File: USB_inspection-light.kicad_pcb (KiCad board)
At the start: 2 copper layers, 82.8 x 13 mm, 24 parts, among them CON1 USB-MINI-B, IC1 MADW__ATTINY13-MM, Q1 MOSFET_N, SW1 SW_PUSH, SW2 SW_PUSH

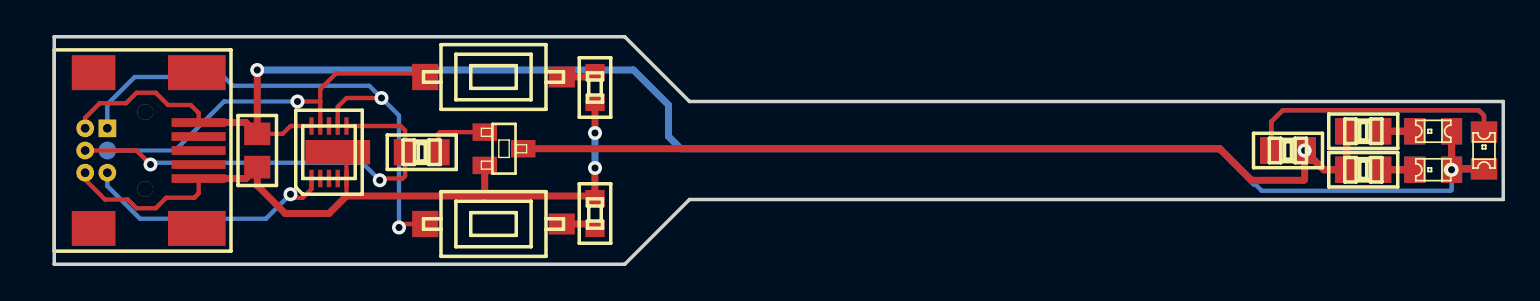
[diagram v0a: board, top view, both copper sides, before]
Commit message: Added a GND plane on F_Cu. Just for fun.
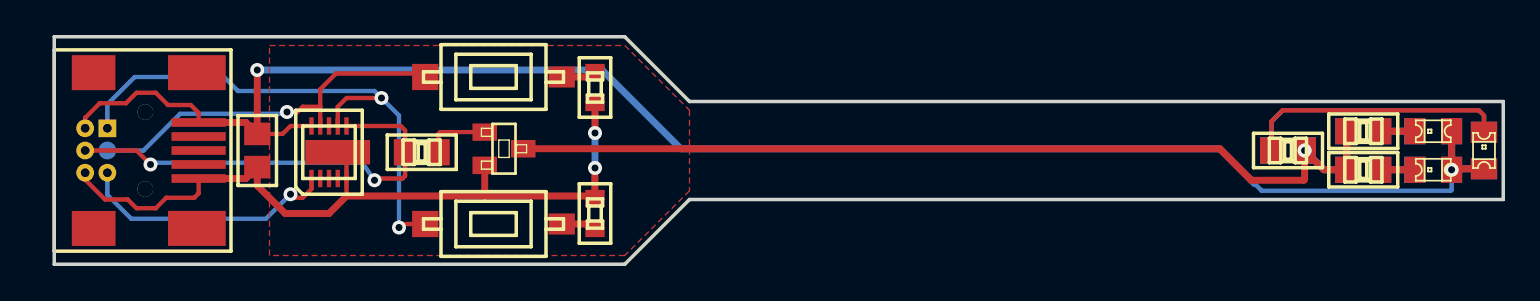
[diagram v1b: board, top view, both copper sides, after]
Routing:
- net +5V: track 101.5 -> 100.5 mm
- added copper zone on F.Cu, net GND
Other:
- board text added: "V0.10.b"
- board text removed: "V0.10.a"

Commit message: GND plane tweaks.
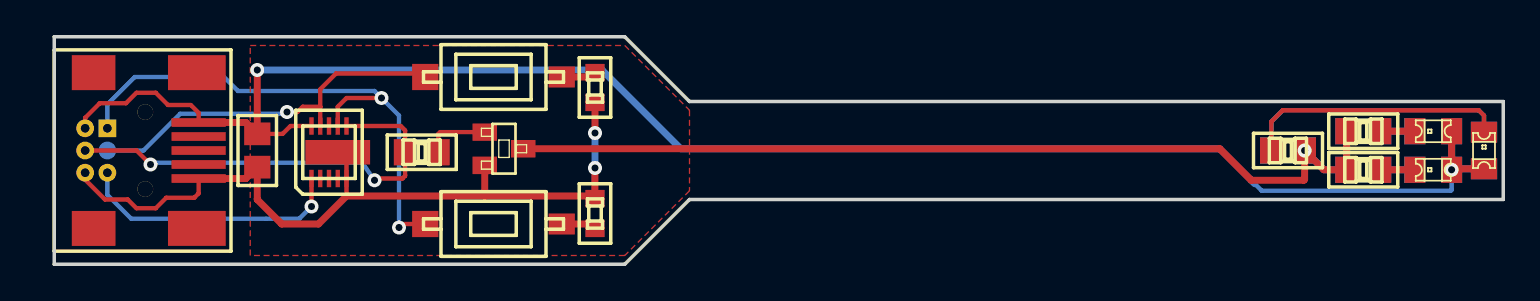
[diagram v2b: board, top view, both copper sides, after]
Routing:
- net GND: track 46.0 -> 46.9 mm
- net /RESET: track 15.0 -> 15.7 mm
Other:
- board text added: "V0.10.c"
- board text removed: "V0.10.b"
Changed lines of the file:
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@@
-(kicad_pcb (version 3) (host pcbnew "(2014-03-01 BZR 4730)-product")
+(kicad_pcb (version 3) (host pcbnew "(2014-02-28 BZR 4729)-product")
   (general
     (links 38)
@@
     (thickness 1.6)
     (drawings 12)
-    (tracks 149)
+    (tracks 148)
     (zones 0)
     (modules 24)
@@
   (title_block
     (title "USB inspection light")
-    (date "02 Mar 2014")
-    (rev 0.10.b)
+    (date "03 Mar 2014")
+    (rev 0.10.c)
     (company "2014 - blog.spitzenpfeil.org")
   )
@@
   )
   (setup
-    (last_trace_width 0.4)
+    (last_trace_width 0.25)
     (user_trace_width 0.25)
     (user_trace_width 0.5)
@@
   (gr_line (start 60.8 102) (end 64.5 105.7) (angle 90) (layer Edge.Cuts) (width 0.2))
   (gr_line (start 111 111.3) (end 111 105.7) (angle 90) (layer Edge.Cuts) (width 0.2))
-  (gr_text V0.10.b (at 78.2 109.9) (layer B.SilkS)
+  (gr_text V0.10.c (at 78.2 109.9) (layer B.SilkS)
     (effects (font (size 1.5 1.5) (thickness 0.3)) (justify mirror))
   )
@@
   (segment (start 48.25004 107.35004) (end 48.25004 108.6) (width 0.25) (layer F.Cu) (net 3) (status 20))
   (segment (start 48 107.1) (end 48.25004 107.35004) (width 0.25) (layer F.Cu) (net 3))
-  (segment (start 31.235 109.77) (end 31.235 111.035) (width 0.25) (layer B.Cu) (net 4) (status 10))
-  (segment (start 42.9 110.7) (end 42.9 110.1) (width 0.25) (layer F.Cu) (net 4) (status 20))
-  (segment (start 42.4 111.2) (end 42.9 110.7) (width 0.25) (layer F.Cu) (net 4))
-  (segment (start 41.9 111.2) (end 42.4 111.2) (width 0.25) (layer F.Cu) (net 4))
-  (segment (start 41.7 111) (end 41.9 111.2) (width 0.25) (layer F.Cu) (net 4))
-  (via (at 41.7 111) (size 0.8) (layers F.Cu B.Cu) (net 4))
-  (segment (start 40.3 112.4) (end 41.7 111) (width 0.25) (layer B.Cu) (net 4))
+  (segment (start 42.9 111.7) (end 42.9 110.1) (width 0.25) (layer F.Cu) (net 4))
+  (segment (start 40.3 112.4) (end 42.2 112.4) (width 0.25) (layer B.Cu) (net 4))
+  (segment (start 31.235 111.035) (end 32.6 112.4) (width 0.25) (layer B.Cu) (net 4))
   (segment (start 32.6 112.4) (end 40.3 112.4) (width 0.25) (layer B.Cu) (net 4))
-  (segment (start 31.235 111.035) (end 32.6 112.4) (width 0.25) (layer B.Cu) (net 4))
+  (via (at 42.9 111.7) (size 0.8) (layers F.Cu B.Cu) (net 4))
+  (segment (start 43.1 111.9) (end 42.9 111.7) (width 0.25) (layer F.Cu) (net 4))
+  (segment (start 31.235 111.035) (end 31.235 109.77) (width 0.25) (layer B.Cu) (net 4) (status 10))
+  (segment (start 42.2 112.4) (end 42.9 111.7) (width 0.25) (layer B.Cu) (net 4))
   (segment (start 31.235 108.5) (end 33.3 108.5) (width 0.25) (layer B.Cu) (net 5) (status 10))
   (segment (start 41.5 106.3) (end 42.1 106.3) (width 0.25) (layer F.Cu) (net 5))
@@
   (segment (start 43.4 106) (end 43.4 107.1) (width 0.25) (layer F.Cu) (net 5) (status 20))
   (segment (start 59.1 105.74836) (end 59.1 107.5) (width 0.4) (layer F.Cu) (net 6) (status 10))
-  (segment (start 39.8 109.44996) (end 39.8 110.5) (width 0.4) (layer F.Cu) (net 6) (status 10))
-  (segment (start 43.9 112.1) (end 44.9 111.1) (width 0.4) (layer F.Cu) (net 6))
-  (segment (start 41.4 112.1) (end 43.9 112.1) (width 0.4) (layer F.Cu) (net 6))
-  (segment (start 39.8 110.5) (end 41.4 112.1) (width 0.4) (layer F.Cu) (net 6))
+  (segment (start 39.8 109.44996) (end 39.8 111.3) (width 0.4) (layer F.Cu) (net 6) (status 10))
+  (segment (start 43.3 112.7) (end 44.9 111.1) (width 0.4) (layer F.Cu) (net 6))
+  (segment (start 41.2 112.7) (end 43.3 112.7) (width 0.4) (layer F.Cu) (net 6))
+  (segment (start 39.8 111.3) (end 41.2 112.7) (width 0.4) (layer F.Cu) (net 6))
   (segment (start 36.45022 110.10152) (end 39.14844 110.10152) (width 0.4) (layer F.Cu) (net 6) (status 10))
   (segment (start 39.14844 110.10152) (end 39.8 109.44996) (width 0.4) (layer F.Cu) (net 6) (status 20))
@@
     (polygon
       (pts
-        (xy 40.5 102.5) (xy 60.8 102.5) (xy 64.5 106.2) (xy 64.5 106.2) (xy 64.5 110.8)
-        (xy 60.8 114.5) (xy 40.5 114.5)
+        (xy 39.4 102.5) (xy 60.8 102.5) (xy 64.5 106.2) (xy 64.5 106.2) (xy 64.5 110.8)
+        (xy 60.8 114.5) (xy 39.4 114.5)
       )
     )

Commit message: Adapted board outline to changed usb socket footprint outline.
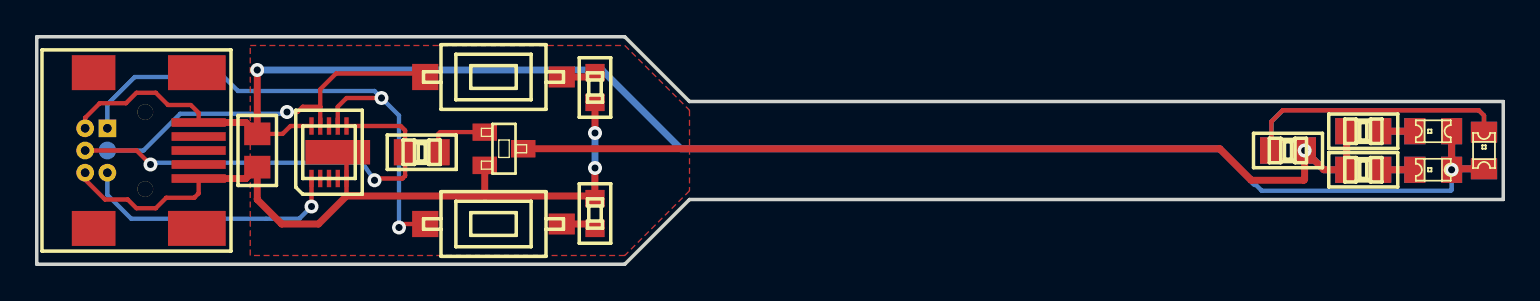
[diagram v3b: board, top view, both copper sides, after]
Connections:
- CON1 pad 2: (no net) -> Net-(CON1-Pad2)
- CON1 pad 3: (no net) -> Net-(CON1-Pad3)
- CON1 pad 4: (no net) -> Net-(CON1-Pad4)
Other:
- board size 82.8 x 13 mm -> 83.8 x 13 mm
- board text added: "V0.10.d"
- board text removed: "V0.10.c"

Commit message: Switched SOT23 footprint to my own library. Silkscreen issue.
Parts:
- Q1: footprint -SOT23C -> my_parts:MADW__SOT23
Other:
- board text added: "V0.10.e"
- board text removed: "V0.10.d"
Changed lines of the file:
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@@
-(kicad_pcb (version 3) (host pcbnew "(2014-03-14 BZR 4749)-product")
+(kicad_pcb (version 3) (host pcbnew "(2014-03-16 BZR 4752)-product")
   (general
     (links 38)
@@
   (title_block
     (title "USB inspection light")
-    (date "14 Mar 2014")
-    (rev 0.10.d)
+    (date "16 Mar 2014")
+    (rev 0.10.e)
     (company "2014 - blog.spitzenpfeil.org")
   )
@@
       (effects (font (size 1 1) (thickness 0.2)) (justify mirror))
     )
-    (fp_text value ISP (at -1.53 2.73 540) (layer B.SilkS) hide
+    (fp_text value ISP (at 3.2 0 540) (layer B.SilkS)
       (effects (font (size 1 1) (thickness 0.2)) (justify mirror))
     )
@@
     (pad 6 thru_hole circle (at 1.27 0.635 270) (size 1.016 1.016) (drill 0.5) (layers *.Cu B.SilkS B.Mask)
       (net 6 GND))
-  )
-  (module -SOT23C (layer F.Cu)
-    (at 53.9 108.4 270)
-    (descr "SMALL OUTLINE TRANSISTOR")
-    (tags "SMALL OUTLINE TRANSISTOR")
-    (attr smd)
-    (fp_text reference Q1 (at 0 -3.05 270) (layer B.SilkS) hide
-      (effects (font (size 1 1) (thickness 0.2)))
-    )
-    (fp_text value MOSFET_N (at 0 3.25 270) (layer B.SilkS) hide
-      (effects (font (size 1 1) (thickness 0.2)))
-    )
-    (fp_line (start -0.2286 -0.7112) (end 0.2286 -0.7112) (layer F.SilkS) (width 0.06604))
-    (fp_line (start 0.2286 -0.7112) (end 0.2286 -1.29286) (layer F.SilkS) (width 0.06604))
-    (fp_line (start -0.2286 -1.29286) (end 0.2286 -1.29286) (layer F.SilkS) (width 0.06604))
-    (fp_line (start -0.2286 -0.7112) (end -0.2286 -1.29286) (layer F.SilkS) (width 0.06604))
-    (fp_line (start 0.7112 1.29286) (end 1.1684 1.29286) (layer F.SilkS) (width 0.06604))
-    (fp_line (start 1.1684 1.29286) (end 1.1684 0.7112) (layer F.SilkS) (width 0.06604))
-    (fp_line (start 0.7112 0.7112) (end 1.1684 0.7112) (layer F.SilkS) (width 0.06604))
-    (fp_line (start 0.7112 1.29286) (end 0.7112 0.7112) (layer F.SilkS) (width 0.06604))
-    (fp_line (start -1.1684 1.29286) (end -0.7112 1.29286) (layer F.SilkS) (width 0.06604))
-    (fp_line (start -0.7112 1.29286) (end -0.7112 0.7112) (layer F.SilkS) (width 0.06604))
-    (fp_line (start -1.1684 0.7112) (end -0.7112 0.7112) (layer F.SilkS) (width 0.06604))
-    (fp_line (start -1.1684 1.29286) (end -1.1684 0.7112) (layer F.SilkS) (width 0.06604))
-    (fp_line (start -0.49784 0.29972) (end 0.49784 0.29972) (layer F.SilkS) (width 0.06604))
-    (fp_line (start 0.49784 0.29972) (end 0.49784 -0.29972) (layer F.SilkS) (width 0.06604))
-    (fp_line (start -0.49784 -0.29972) (end 0.49784 -0.29972) (layer F.SilkS) (width 0.06604))
-    (fp_line (start -0.49784 0.29972) (end -0.49784 -0.29972) (layer F.SilkS) (width 0.06604))
-    (fp_line (start 1.41986 -0.65786) (end 1.41986 0.65786) (layer F.SilkS) (width 0.1524))
-    (fp_line (start 1.41986 0.65786) (end -1.41986 0.65786) (layer F.SilkS) (width 0.1524))
-    (fp_line (start -1.41986 0.65786) (end -1.41986 -0.65786) (layer F.SilkS) (width 0.1524))
-    (fp_line (start -1.41986 -0.65786) (end 1.41986 -0.65786) (layer F.SilkS) (width 0.1524))
-    (pad 1 smd rect (at -0.94996 1.09982 270) (size 0.99822 1.39954) (layers F.Cu F.Mask)
-      (net 21 "Net-(Q1-Pad1)"))
-    (pad 2 smd rect (at 0.94996 1.09982 270) (size 0.99822 1.39954) (layers F.Cu F.Mask)
-      (net 6 GND))
-    (pad 3 smd rect (at 0 -1.09982 270) (size 0.99822 1.39954) (layers F.Cu F.Mask)
-      (net 22 "Net-(Q1-Pad3)"))
-    (model ../../../../../Arduino/KiCAD/kicad_sources/library-repos/kicad-library/modules/packages3d/smd/smd_transistors/sot23.wrl
-      (at (xyz 0 0 0))
-      (scale (xyz 1 1 1))
-      (rotate (xyz 0 0 0))
-    )
   )
   (module OSHW-logo_silkscreen_4mm (layer B.Cu)
@@
     (tags CAPACITOR)
     (attr smd)
-    (fp_text reference C1 (at 2.77 -0.12 360) (layer F.SilkS) hide
+    (fp_text reference C1 (at -2.9 0 360) (layer F.SilkS)
       (effects (font (size 1 1) (thickness 0.2)))
     )
@@
     (tags RESISTOR)
     (attr smd)
-    (fp_text reference R7 (at 0 -1.7) (layer F.SilkS) hide
+    (fp_text reference R7 (at -0.2 -1.8) (layer F.SilkS)
       (effects (font (size 1 1) (thickness 0.2)))
     )
@@
     (tags RESISTOR)
     (attr smd)
-    (fp_text reference R8 (at 0 -1.9 90) (layer F.SilkS) hide
+    (fp_text reference R8 (at 0 2.1 360) (layer F.SilkS)
       (effects (font (size 1 1) (thickness 0.2)))
     )
@@
     (tags RESISTOR)
     (attr smd)
-    (fp_text reference R9 (at 0 -1.9 270) (layer F.SilkS) hide
+    (fp_text reference R9 (at 0 -2.1 360) (layer F.SilkS)
       (effects (font (size 1 1) (thickness 0.2)))
     )
@@
     )
   )
+  (module my_parts:MADW__SOT23 (layer F.Cu)
+    (at 53.9 108.4 270)
+    (descr "SMALL OUTLINE TRANSISTOR")
+    (tags "SMALL OUTLINE TRANSISTOR")
+    (attr smd)
+    (fp_text reference Q1 (at 0 -3.6 540) (layer F.SilkS)
+      (effects (font (size 1 1) (thickness 0.2)))
+    )
+    (fp_text value MOSFET_N (at 0 3.2 270) (layer F.SilkS) hide
+      (effects (font (size 1 1) (thickness 0.2)))
+    )
+    (fp_line (start 1.9 -2.2) (end 1.9 2.2) (layer F.SilkS) (width 0.2))
+    (fp_line (start 1.9 2.2) (end -1.9 2.2) (layer F.SilkS) (width 0.2))
+    (fp_line (start -1.9 2.2) (end -1.9 -2.2) (layer F.SilkS) (width 0.2))
+    (fp_line (start -1.9 -2.2) (end 1.9 -2.2) (layer F.SilkS) (width 0.2))
+    (fp_line (start -0.2286 -0.7112) (end 0.2286 -0.7112) (layer F.SilkS) (width 0.2))
+    (fp_line (start 0.2286 -0.7112) (end 0.2286 -1.29286) (layer F.SilkS) (width 0.2))
+    (fp_line (start -0.2286 -1.29286) (end 0.2286 -1.29286) (layer F.SilkS) (width 0.2))
+    (fp_line (start -0.2286 -0.7112) (end -0.2286 -1.29286) (layer F.SilkS) (width 0.2))
+    (fp_line (start 0.7112 1.29286) (end 1.1684 1.29286) (layer F.SilkS) (width 0.2))
+    (fp_line (start 1.1684 1.29286) (end 1.1684 0.7112) (layer F.SilkS) (width 0.2))
+    (fp_line (start 0.7112 0.7112) (end 1.1684 0.7112) (layer F.SilkS) (width 0.2))
+    (fp_line (start 0.7112 1.29286) (end 0.7112 0.7112) (layer F.SilkS) (width 0.2))
+    (fp_line (start -1.1684 1.29286) (end -0.7112 1.29286) (layer F.SilkS) (width 0.2))
+    (fp_line (start -0.7112 1.29286) (end -0.7112 0.7112) (layer F.SilkS) (width 0.2))
+    (fp_line (start -1.1684 0.7112) (end -0.7112 0.7112) (layer F.SilkS) (width 0.2))
+    (fp_line (start -1.1684 1.29286) (end -1.1684 0.7112) (layer F.SilkS) (width 0.2))
+    (fp_line (start -0.49784 0.29972) (end 0.49784 0.29972) (layer F.SilkS) (width 0.2))
+    (fp_line (start 0.49784 0.29972) (end 0.49784 -0.29972) (layer F.SilkS) (width 0.2))
+    (fp_line (start -0.49784 -0.29972) (end 0.49784 -0.29972) (layer F.SilkS) (width 0.2))
+    (fp_line (start -0.49784 0.29972) (end -0.49784 -0.29972) (layer F.SilkS) (width 0.2))
+    (fp_line (start 1.41986 -0.65786) (end 1.41986 0.65786) (layer F.SilkS) (width 0.2))
+    (fp_line (start 1.41986 0.65786) (end -1.41986 0.65786) (layer F.SilkS) (width 0.2))
+    (fp_line (start -1.41986 0.65786) (end -1.41986 -0.65786) (layer F.SilkS) (width 0.2))
+    (fp_line (start -1.41986 -0.65786) (end 1.41986 -0.65786) (layer F.SilkS) (width 0.2))
+    (pad 1 smd rect (at -0.95 1.1 270) (size 1 1.4) (layers F.Cu F.Mask)
+      (net 21 "Net-(Q1-Pad1)"))
+    (pad 2 smd rect (at 0.95 1.1 270) (size 1 1.4) (layers F.Cu F.Mask)
+      (net 6 GND))
+    (pad 3 smd rect (at 0 -1.1 270) (size 1 1.4) (layers F.Cu F.Mask)
+      (net 22 "Net-(Q1-Pad3)"))
+  )
   (gr_line (start 27.2 115) (end 60.8 115) (angle 90) (layer Edge.Cuts) (width 0.2))
   (gr_line (start 27.2 102) (end 60.8 102) (angle 90) (layer Edge.Cuts) (width 0.2))
@@
   (gr_line (start 60.8 102) (end 64.5 105.7) (angle 90) (layer Edge.Cuts) (width 0.2))
   (gr_line (start 111 111.3) (end 111 105.7) (angle 90) (layer Edge.Cuts) (width 0.2))
-  (gr_text V0.10.d (at 78.2 109.9) (layer B.SilkS)
+  (gr_text V0.10.e (at 78.2 109.9) (layer B.SilkS)
     (effects (font (size 1.5 1.5) (thickness 0.3)) (justify mirror))
   )

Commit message: Tweaks: incr. trace-width, ISP header, copper pour.
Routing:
- net /PWM: track 25.3 -> 34.6 mm, vias 2 -> 1
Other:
- board text added: "V0.10.f"
- board text removed: "V0.10.e"

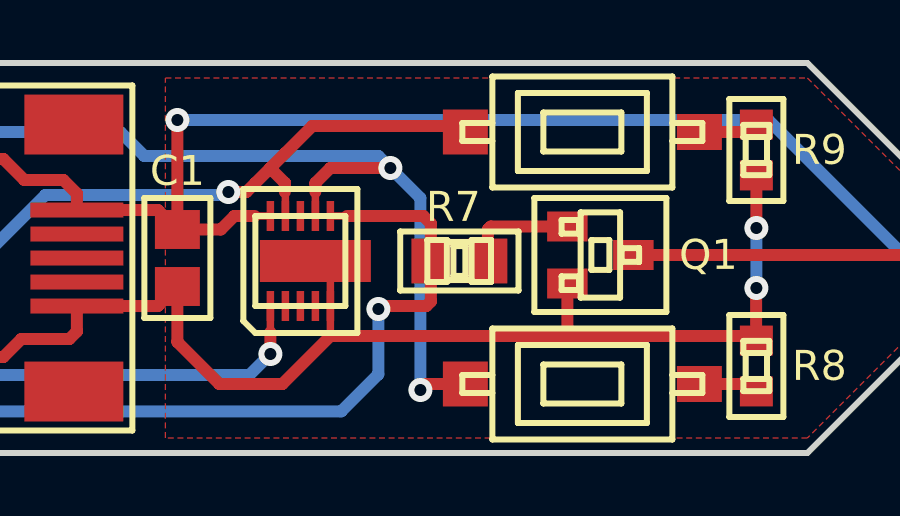
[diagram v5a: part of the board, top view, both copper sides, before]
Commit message: Added 100k pull-down resistor to mosfet gate.
Purpose: prevent LED flash on power-up.
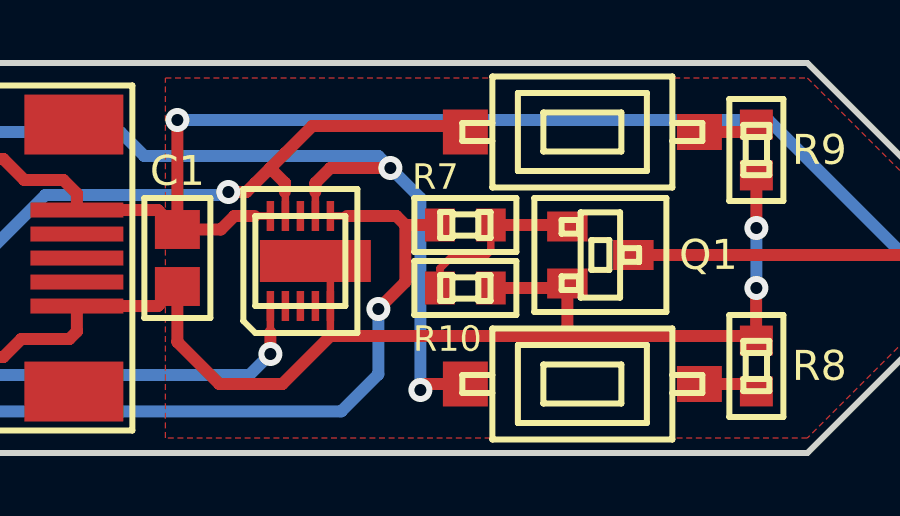
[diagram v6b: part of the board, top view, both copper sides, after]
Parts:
- added R10: 100k, my_parts:MADW__R0603_2, F.Cu at (49.4, 109.5)
- R7: footprint my_parts:MADW__R0805 -> my_parts:MADW__R0603_2
- moved R7 1.22 mm to (49.4, 107.4)
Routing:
- net Net-(Q1-Pad1): track 3.74 -> 6.67 mm
- net GND: track 46.9 -> 49.5 mm
- net /PWM: track 34.6 -> 33.8 mm
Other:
- board text added: "V0.20.a"
- board text removed: "V0.10.f"
